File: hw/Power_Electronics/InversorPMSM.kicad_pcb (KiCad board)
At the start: 4 copper layers, 150 x 95 mm, 224 parts, among them J1 FROM_CONTROL_BOARD, J2 HALL_CONNECTOR, J5 MEASURE_CONN, Q1 HY1908D, Q2 HY1908D, Q3 HY1908D, Q4 HY1908D, Q5 HY1908D, Q6 HY1908D, U1 STDRIVE601, U2 AMS1117, U3 TSV912IDT, U4 TSV912IDT

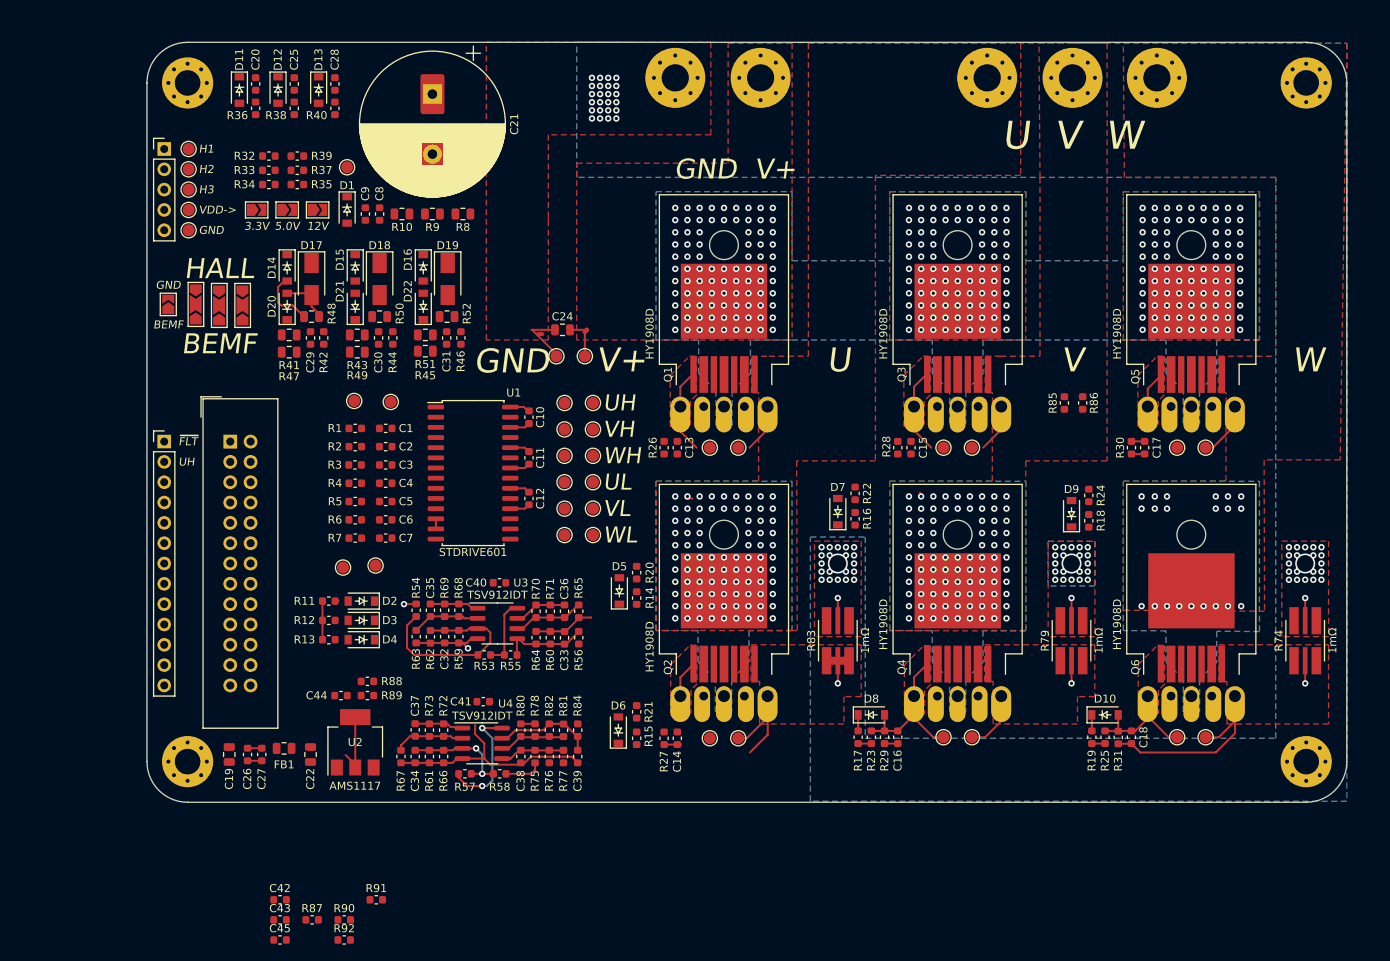
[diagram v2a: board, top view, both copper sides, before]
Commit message: finish power board layout first pass
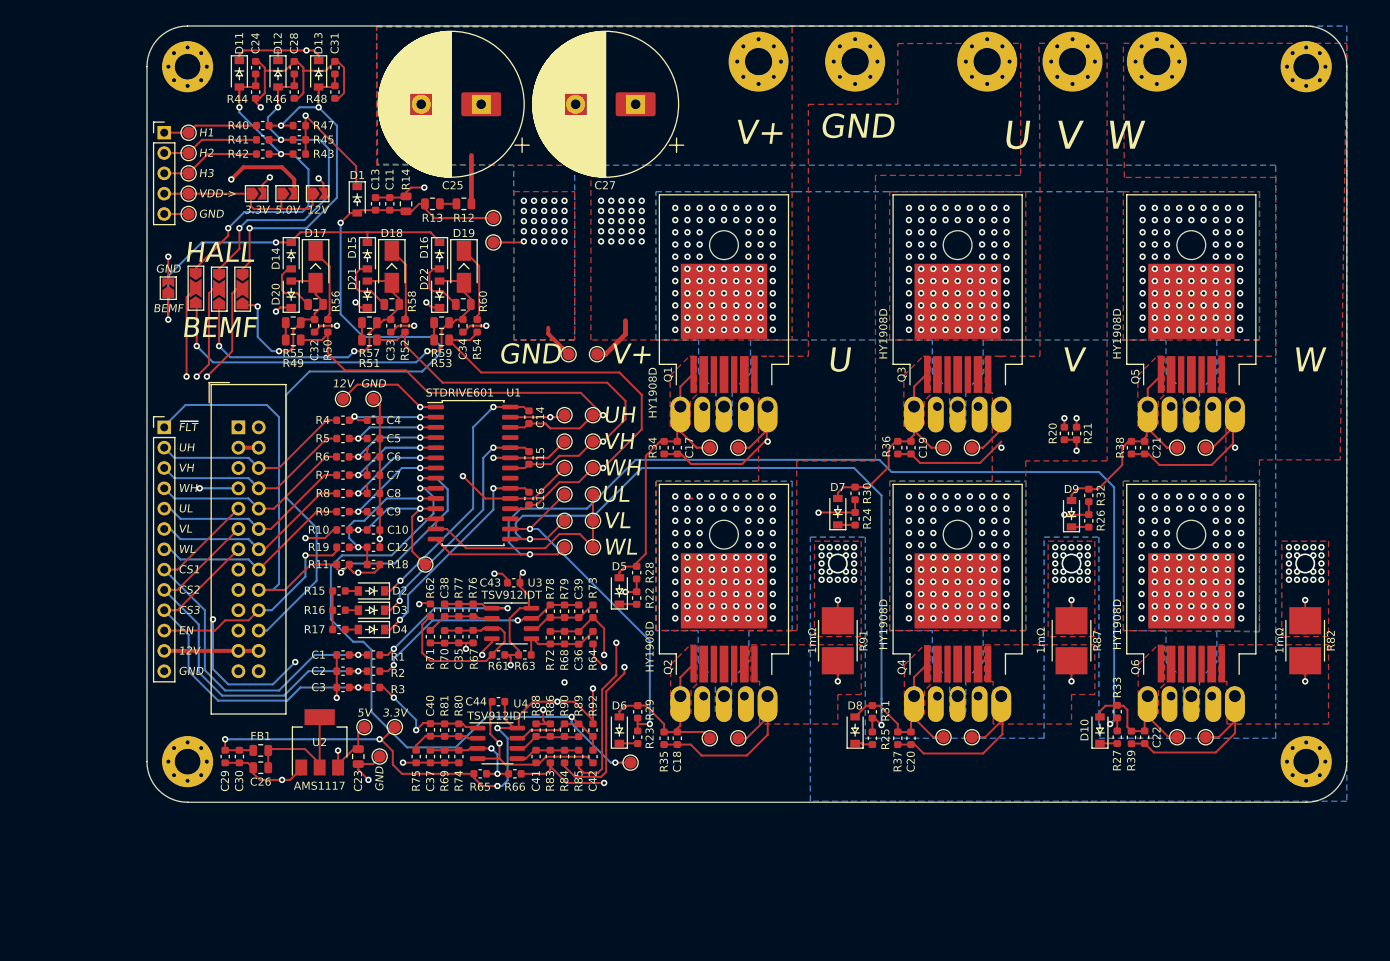
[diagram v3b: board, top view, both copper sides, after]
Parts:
- removed the C24 at (135.6, 97.0)
- removed the R74 at (228.5, 135.9)
- removed the R79 at (199.3, 135.9)
- removed the R83 at (170.1, 135.9)
- added C27: CP, inversor-pmsm:CP_Radial_D18.0mm_P7.50mm_universal, F.Cu at (144.8, 68.8)
- added R82: 1mΩ, inversor-pmsm:R_2512_6332Metric, F.Cu at (228.5, 135.9)
- added R87: 1mΩ, inversor-pmsm:R_2512_6332Metric, F.Cu at (199.3, 135.9)
- added R91: 1mΩ, inversor-pmsm:R_2512_6332Metric, F.Cu at (170.1, 135.9)
- added TP34: TestPoint, TestPoint:TestPoint_Pad_D1.5mm, F.Cu at (110.9, 146.7)
- added TP35: TestPoint, TestPoint:TestPoint_Pad_D1.5mm, F.Cu at (127.0, 86.1)
- added TP38: TestPoint, TestPoint:TestPoint_Pad_D1.5mm, F.Cu at (112.8, 150.4)
- added TP39: TestPoint, TestPoint:TestPoint_Pad_D1.5mm, F.Cu at (114.7, 146.7)
- D17, D18, D19: footprint Diode_SMD:D_SMA -> inversor-pmsm:D_SMA_custom
- moved C12 50.5 mm to (112.0, 124.2)
- moved R19 49.1 mm to (108.2, 124.2)
- moved R11 44.4 mm to (108.2, 126.4), turned to 180 degrees
- moved R18 41.9 mm to (112.0, 126.4), turned to 180 degrees
- moved TP40 40.3 mm to (144.1, 151.1)
- moved R1 34.0 mm to (112.0, 137.7)
- moved C2 32.1 mm to (108.2, 139.7), turned to 180 degrees
- moved C1 31.6 mm to (108.2, 137.7), turned to 180 degrees
- moved H3 22.6 mm to (172.2, 63.5)
- moved TP2 19.4 mm to (127.0, 83.1)
- moved C23 16.1 mm to (110.1, 150.4)
- moved TP1 10.3 mm to (118.5, 126.4)
- moved C26 6.44 mm to (97.9, 151.8), turned to 180 degrees
- moved C25 6.23 mm to (125.5, 68.8), turned to 180 degrees
- moved U2 4.44 mm to (105.3, 148.6)
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- renumbered C42 to C1, C7 to C10, C8 to C11, C45 to C12, C9 to C13, C10 to C14, C11 to C15, C12 to C16, C13 to C17, C14 to C18, C15 to C19, C43 to C2, C16 to C20, C17 to C21, C18 to C22, C19 to C23, C20 to C24, C21 to C25, C22 to C26, C25 to C28, C26 to C29, C44 to C3, C27 to C30, C28 to C31, C29 to C32, C30 to C33, C31 to C34, C32 to C35, C33 to C36, C34 to C37, C35 to C38, C36 to C39, C1 to C4, C37 to C40, C38 to C41, C39 to C42, C40 to C43, C41 to C44, C2 to C5, C3 to C6, C4 to C7, C5 to C8, C6 to C9, H5 to H1, H6 to H2, H7 to H3, H8 to H4, H9 to H5, H1 to H6, H2 to H7, H3 to H8, H4 to H9, J5 to J2, J2 to J3, JP7 to JP4, JP4 to JP5, JP5 to JP6, JP6 to JP7, R87 to R1, R7 to R10, R90 to R11, R8 to R12, R9 to R13, R10 to R14, R11 to R15, R12 to R16, R13 to R17, R91 to R18, R92 to R19, R88 to R2, R85 to R20, R86 to R21, R14 to R22, R15 to R23, R16 to R24, R17 to R25, R18 to R26, R19 to R27, R20 to R28, R21 to R29, R89 to R3, R22 to R30, R23 to R31, R24 to R32, R25 to R33, R26 to R34, R27 to R35, R28 to R36, R29 to R37, R30 to R38, R31 to R39, R1 to R4, R32 to R40, R33 to R41, R34 to R42, R35 to R43, R36 to R44, R37 to R45, R38 to R46, R39 to R47, R40 to R48, R41 to R49, R2 to R5, R42 to R50, R43 to R51, R44 to R52, R45 to R53, R46 to R54, R47 to R55, R48 to R56, R49 to R57, R50 to R58, R51 to R59, R3 to R6, R52 to R60, R53 to R61, R54 to R62, R55 to R63, R56 to R64, R57 to R65, R58 to R66, R59 to R67, R60 to R68, R61 to R69, R4 to R7, R62 to R70, R63 to R71, R64 to R72, R65 to R73, R66 to R74, R67 to R75, R68 to R76, R69 to R77, R70 to R78, R71 to R79, R5 to R8, R72 to R80, R73 to R81, R75 to R83, R76 to R84, R77 to R85, R78 to R86, R80 to R88, R81 to R89, R6 to R9, R82 to R90, R84 to R92, TP9 to TP10, TP10 to TP11, TP11 to TP12, TP12 to TP13, TP13 to TP14, TP14 to TP15, TP15 to TP16, TP16 to TP17, TP17 to TP18, TP18 to TP19, TP3 to TP2, TP19 to TP20, TP20 to TP21, TP21 to TP22, TP22 to TP23, TP23 to TP24, TP24 to TP25, TP25 to TP26, TP26 to TP27, TP27 to TP28, TP32 to TP29, TP2 to TP3, TP33 to TP30, TP34 to TP31, TP35 to TP32, TP36 to TP33, TP28 to TP36, TP29 to TP37, TP30 to TP40, TP31 to TP7, TP7 to TP8, TP8 to TP9
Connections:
- C1 pad 1: SENSE1 -> SENSE_OUT1F
- C1 pad 2: SENSE1_REF -> GND
- C10 pad 2: SENSE1_REF -> GND
- C11 pad 2: SENSE1_REF -> GND
- C12 pad 2: SENSE1_REF -> GND
- C13 pad 2: SENSE1_REF -> GND
- C2 pad 1: SENSE2 -> SENSE_OUT2F
- C2 pad 2: SENSE1_REF -> GND
- C23 pad 2: SENSE1_REF -> GND
- C24 pad 1: SENSE1_REF -> GND
- C25 pad 2: SENSE1_REF -> GND
- C26 pad 2: SENSE1_REF -> GND
- C28 pad 1: SENSE1_REF -> GND
- C29 pad 2: SENSE1_REF -> GND
- C3 pad 1: SENSE3 -> SENSE_OUT3F
- C3 pad 2: SENSE1_REF -> GND
- C30 pad 2: SENSE1_REF -> GND
- C31 pad 1: SENSE1_REF -> GND
- C32 pad 1: SENSE1_REF -> GND
- C33 pad 1: SENSE1_REF -> GND
- C34 pad 1: SENSE1_REF -> GND
- C36 pad 2: SENSE1_REF -> SENSE2_REF
- C37 pad 2: SENSE1_REF -> SENSE3_REF
- C4 pad 2: SENSE1_REF -> GND
- C41 pad 2: SENSE1_REF -> GND
- C42 pad 2: SENSE1_REF -> GND
- C43 pad 2: SENSE1_REF -> GND
- C44 pad 2: SENSE1_REF -> GND
- C5 pad 2: SENSE1_REF -> GND
- C6 pad 2: SENSE1_REF -> GND
- C7 pad 2: SENSE1_REF -> GND
- C8 pad 2: SENSE1_REF -> GND
- C9 pad 2: SENSE1_REF -> GND
- H3 pad 1: SENSE1_REF -> GND
- H6 pad 1: SENSE1_REF -> GND
- H7 pad 1: SENSE1_REF -> GND
- H8 pad 1: SENSE1_REF -> GND
- H9 pad 1: SENSE1_REF -> GND
- J1 pad 1: SENSE1_REF -> GND
- J1 pad 11: SENSE2 -> SENSE_OUT2F
- J1 pad 13: SENSE3 -> SENSE_OUT3F
- J1 pad 2: SENSE1_REF -> GND
- J1 pad 25: SENSE1_REF -> GND
- J1 pad 26: SENSE1_REF -> GND
- J1 pad 9: SENSE1 -> SENSE_OUT1F
- J2 pad 1: ~ERROR -> ~FAULT
- J2 pad 10: SENSE3 -> SENSE_OUT3F
- J2 pad 13: SENSE1_REF -> GND
- J2 pad 8: SENSE1 -> SENSE_OUT1F
- J2 pad 9: SENSE2 -> SENSE_OUT2F
- J3 pad 5: SENSE1_REF -> GND
- JP4 pad 2: SENSE1_REF -> GND
- R1 pad 1: SENSE1 -> SENSE_OUT1F
- R14 pad 2: SENSE1_REF -> GND
- R2 pad 1: SENSE2 -> SENSE_OUT2F
- R20 pad 1: +3V3 -> NTC_TEMP
- R20 pad 2: NTC_TEMP -> GND
- R21 pad 1: NTC_TEMP -> +3V3
- R21 pad 2: SENSE1_REF -> NTC_TEMP
- R3 pad 1: SENSE3 -> SENSE_OUT3F
- R44 pad 2: SENSE1_REF -> GND
- R46 pad 2: SENSE1_REF -> GND
- R48 pad 2: SENSE1_REF -> GND
- R62 pad 2: SENSE1 -> SENSE1_SIG
- R64 pad 2: SENSE2 -> SENSE2_SIG
- R66 pad 2: SENSE3 -> SENSE3_SIG
- R68 pad 2: SENSE1_REF -> SENSE2_REF
- R69 pad 2: SENSE1_REF -> SENSE3_REF
- R72 pad 2: SENSE1_REF -> SENSE2_REF
- R73 pad 2: SENSE1_REF -> SENSE2_REF
- R74 pad 2: SENSE1_REF -> SENSE3_REF
- R75 pad 2: SENSE1_REF -> SENSE3_REF
- R83 pad 2: SENSE3 -> SENSE3_SIG
- R84 pad 2: SENSE2 -> SENSE2_SIG
- R85 pad 2: SENSE1 -> SENSE1_SIG
- R86 pad 2: SENSE1_REF -> GND
- R88 pad 2: SENSE1_REF -> GND
- TP29 pad 1: SENSE1_REF -> GND
- TP37 pad 1: SENSE1_REF -> GND
- TP4 pad 1: SENSE1_REF -> GND
- TP5 pad 1: SENSE1_REF -> GND
- TP6 pad 1: SENSE1_REF -> GND
- TP7 pad 1: SENSE1_REF -> GND
- U1 pad 12: SENSE1_REF -> GND
- U1 pad 13: SENSE1_REF -> GND
- U2 pad 1: SENSE1_REF -> GND
- U3 pad 4: SENSE1_REF -> GND
- U4 pad 4: SENSE1_REF -> GND
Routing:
- net +3V3: track 27.0 -> 483.6 mm, vias 2 -> 16
- net GND: track 0.00 -> 332.4 mm, vias 0 -> 105
- net NTC_TEMP: track 0.00 -> 249.1 mm, vias 0 -> 4
- net OUT3: track 8.47 -> 158.3 mm, vias 21 -> 92
- net SENSE3_REF: track 0.00 -> 138.4 mm, vias 0 -> 2
- net Net-(R27-Pad2): track 1.69 -> 136.0 mm, vias 0 -> 2
- net +12V: track 0.00 -> 128.6 mm, vias 0 -> 3
- net +5V: track 1.02 -> 121.2 mm, vias 0 -> 2
- net OUT2: track 6.77 -> 125.6 mm, vias 90 -> 92
- net Net-(R26-Pad2): track 0.00 -> 118.0 mm, vias 0 -> 2
- net SENSE3_SIG: track 0.00 -> 107.6 mm, vias 0 -> 2
- net VBUS_SCALED: track 0.00 -> 103.9 mm, vias 0 -> 1
- net OUT1: track 10.8 -> 105.9 mm, vias 90 -> 92
- net Net-(R25-Pad2): track 1.79 -> 93.2 mm, vias 0 -> 2
- net SENSE2_SIG: track 0.00 -> 88.9 mm, vias 0 -> 3
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- added copper zone on B.Cu, net GND
- added copper zone on F.Cu, net GND
- added copper zone on In1.Cu, net GND
- removed copper zone on B.Cu, net SENSE1_REF
- removed copper zone on F.Cu, net SENSE1_REF
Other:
- board size 150 x 95 mm -> 150 x 97 mm
- board text added: "5V"
- board text added: "CS1"
- board text added: "CS2"
- board text added: "CS3"
- board text added: "EN"
- board text removed: "GND V+"

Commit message: adjustments made on silkscreen layer
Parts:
- added J6: POWER_INPUT, inversor-pmsm:Amass_XT60PW-M_Kombifootprint, F.Cu at (141.1, 74.4)
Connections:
- R82 pad 1: SENSE3_REF -> GND
- R82 pad 4: SENSE3_SIG -> SENSE3
- R87 pad 1: SENSE2_REF -> GND
- R87 pad 4: SENSE2_SIG -> SENSE2
- R91 pad 1: SENSE1_REF -> GND
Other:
- board text added: "PEGASUS Motor Controller v1 11/2020 GABRIEL GOSMANN PEDRO H. C. KOPPER"

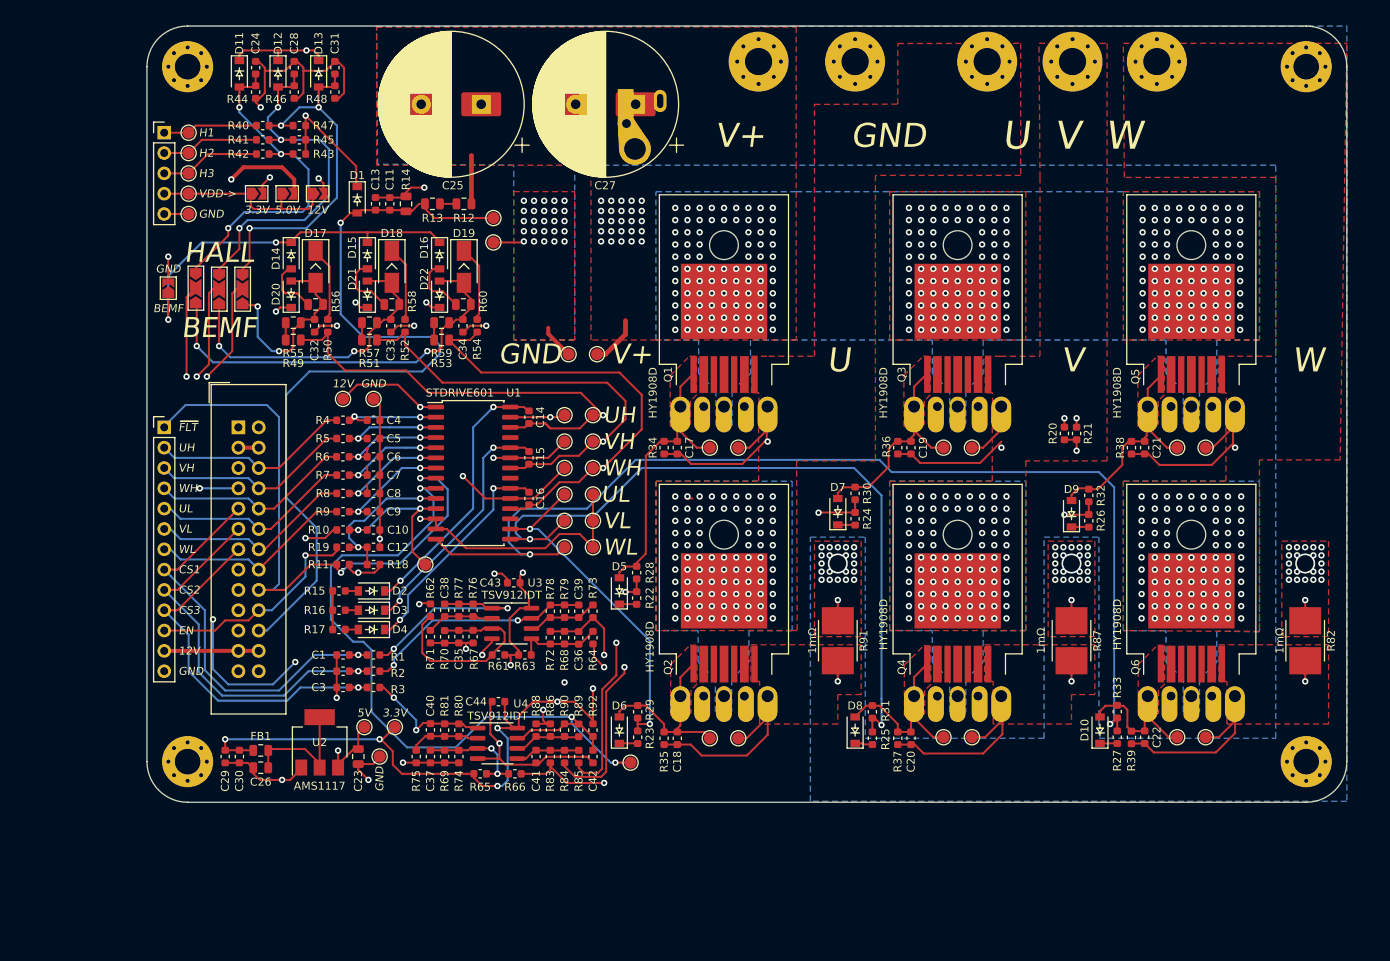
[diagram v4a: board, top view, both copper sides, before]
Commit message: turn power electronics PCB into a 2 layer board
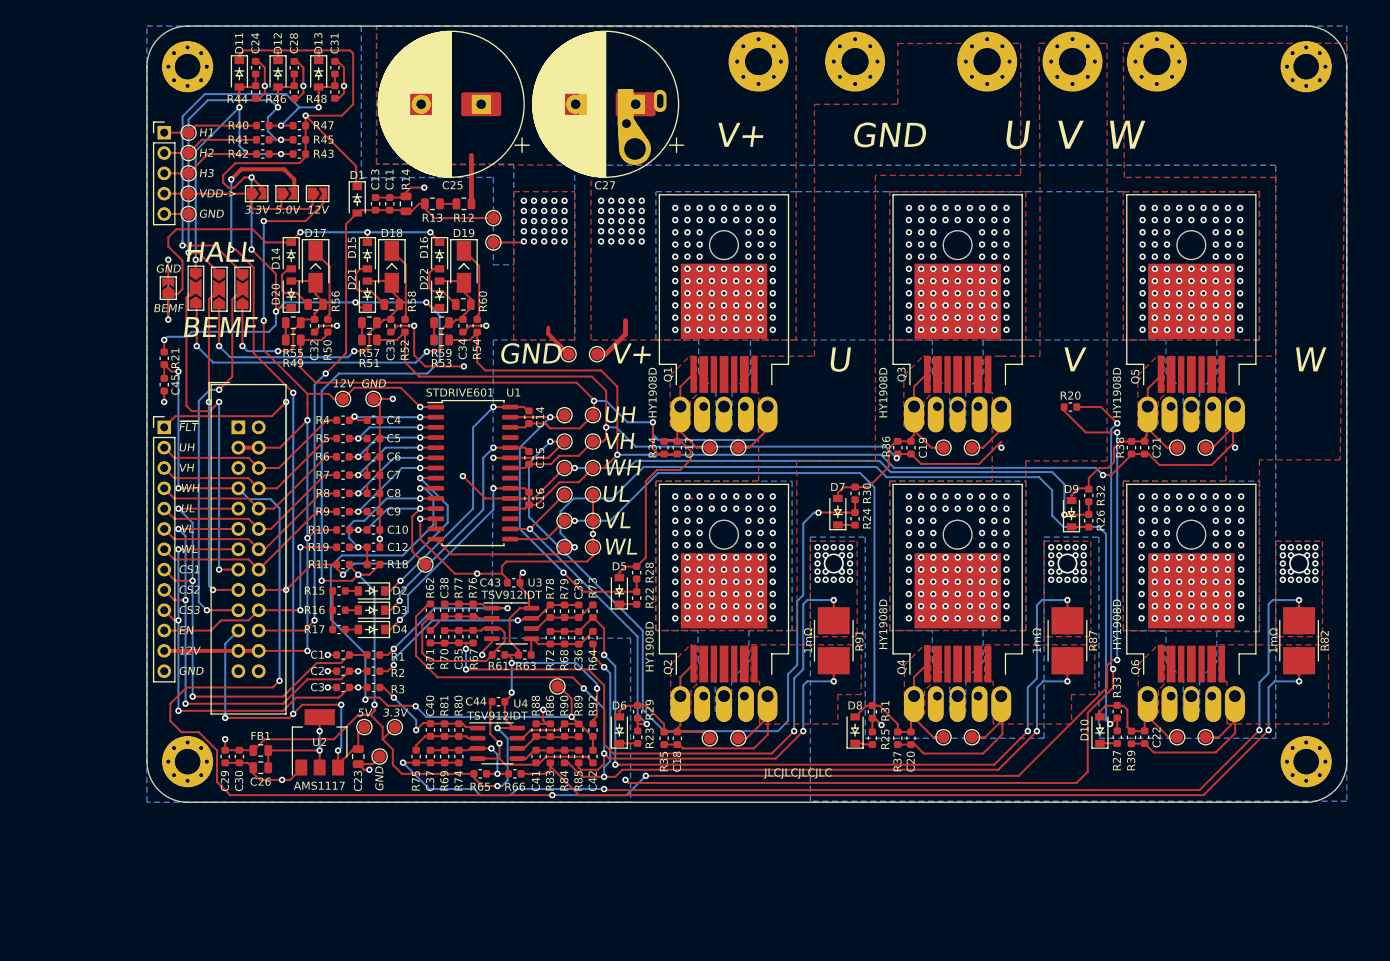
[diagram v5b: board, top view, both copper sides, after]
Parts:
- added C45: 100nF, Capacitor_SMD:C_0603_1608Metric, F.Cu at (85.9, 103.9)
- moved R21 114.4 mm to (85.9, 100.6)
- moved TP40 13.2 mm to (135.0, 141.6)
- moved R20 3.39 mm to (199.1, 106.7), turned to 0 degrees
- moved R82 0.76 mm to (227.7, 135.9)
- moved R87 0.51 mm to (198.8, 135.9)
- moved R91 0.51 mm to (169.5, 135.9)
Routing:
- net +3V3: track 483.6 -> 305.3 mm, vias 16 -> 17
- net GND: track 332.4 -> 288.2 mm, vias 105 -> 114
- net Net-(R26-Pad2): track 118.0 -> 88.0 mm, vias 2 -> 3
- net Net-(R24-Pad2): track 78.5 -> 106.1 mm, vias 2 -> 3
- net VBUS_SCALED: track 103.9 -> 79.4 mm, vias 1 -> 2
- net SENSE2_REF: track 81.0 -> 100.6 mm, vias 2 -> 4
- net OUT3: track 158.3 -> 141.7 mm, vias 92 -> 93
- net OUT2: track 125.6 -> 112.7 mm, vias 92 -> 93
- net SENSE1_REF: track 69.7 -> 82.6 mm, vias 2 -> 4
- net +12V: track 128.6 -> 115.9 mm, vias 3 -> 6
- net ENC_HALL_A: track 45.7 -> 56.4 mm
- net Net-(R25-Pad2): track 93.2 -> 83.1 mm
- net Net-(R27-Pad2): track 136.0 -> 126.2 mm
- net CIN: track 95.7 -> 86.4 mm, vias 3 -> 4
- net SENSE_OUT1F: track 51.4 -> 60.6 mm, vias 1 -> 3
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- removed copper zone on In1.Cu, net GND
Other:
- copper layers 4 -> 2
- board text added: "JLCJLCJLCJLC"

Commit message: adjusts made on mask layer to expose high current path
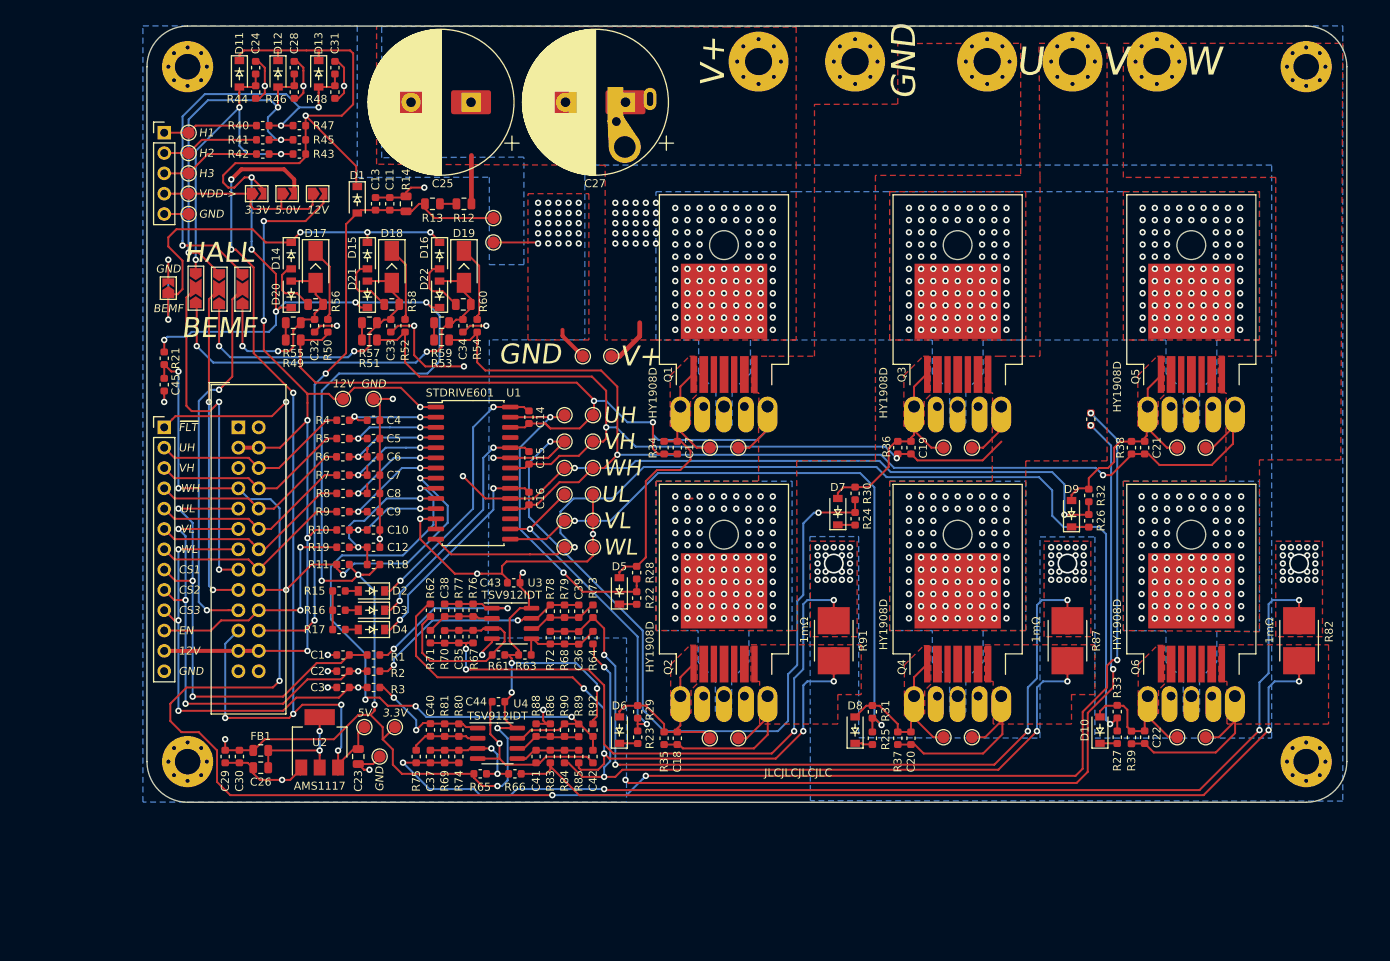
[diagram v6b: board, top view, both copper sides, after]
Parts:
- removed TP1, TP40: TestPoint, TestPoint:TestPoint_Pad_D1.5mm
- added G***: LOGO, inversor-pmsm:pegasus_large, B.Cu at (124.5, 111.0)
- moved R20 2.96 mm to (201.7, 108.2), turned to 270 degrees
- moved TP36 1.80 mm to (141.7, 100.3)
- moved TP37 1.80 mm to (138.2, 100.3)
- moved C27 1.30 mm to (143.5, 68.6)
- moved J6 1.30 mm to (139.8, 74.2)
- moved C25 1.30 mm to (124.2, 68.6)
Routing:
- net Net-(C10-Pad1): track 21.2 -> 13.1 mm
- net CIN: track 86.4 -> 81.6 mm
- net GND: track 288.2 -> 284.8 mm
- net OUT2: track 112.7 -> 112.3 mm, vias 93 -> 92
- net OUT3: vias 93 -> 92
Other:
- board text removed: "U V W"

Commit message: create high voltage net class and solve DRC erros
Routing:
- net OUT1: track 99.8 -> 94.8 mm
- net OUT2: track 112.3 -> 114.8 mm
- net GND: vias 114 -> 102
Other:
- net class HighPower: clearance 0.8 -> 0.6
- net class HighVoltage added: clearance 0.4, trace_width 0.25, via_dia 0.8, via_drill 0.4
- board text added: "PEGASUS Motor Controller v1 11/2020 GABRIEL GOSMANN PEDRO KOPPER"
- board text removed: "PEGASUS Motor Controller v1 11/2020 GABRIEL GOSMANN PEDRO H. C. KOPPER"
